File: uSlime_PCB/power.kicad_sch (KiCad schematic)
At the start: 20 parts, among them CN2 1.25T-2AW, J1 USB_C_Receptacle_USB2.0_14P, U2 MSK-12C02_SMD_SPDT_SWITCH, U3 AP2112K-3.3TRG1, U4 MCP73831T-2ACI/OT

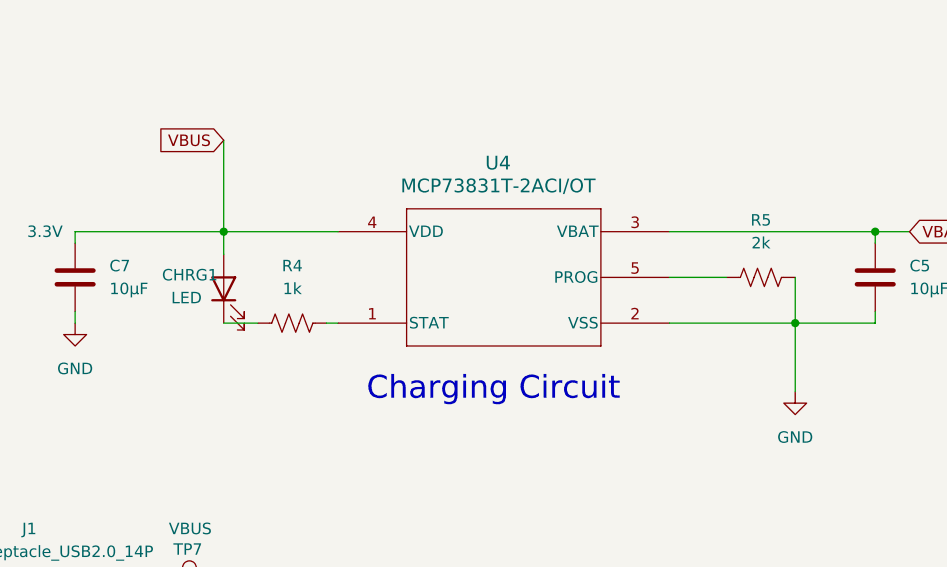
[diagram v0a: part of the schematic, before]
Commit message: v1.0.0 - Use 1206 LED, add resistor pack suggestion
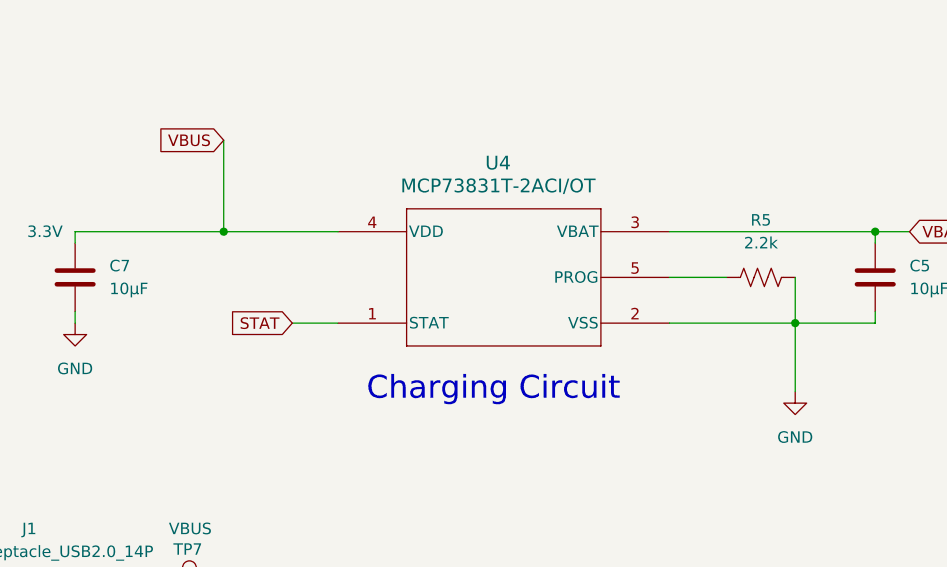
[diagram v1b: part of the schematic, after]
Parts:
- removed CHRG1: LED, LED_SMD:LED_0402_1005Metric, symbol uSlime:LED
- removed R4: 1k, Resistor_SMD:R_0402_1005Metric, symbol uSlime:R_US
- R5: value 2k -> 2.2k
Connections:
- net STAT: now reaches U4.1 (STAT)
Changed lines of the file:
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@@
-	(wire
-		(pts
-			(xy 170.18 87.63) (xy 173.99 87.63)
-		)
-		(stroke
-			(width 0)
-			(type default)
-		)
-	)
 	(wire
 		(pts
@@
 	(wire
 		(pts
-			(xy 181.61 87.63) (xy 182.88 87.63)
+			(xy 177.8 87.63) (xy 182.88 87.63)
 		)
 		(stroke
@@
 			(width 0.1524)
 			(type solid)
-		)
-	)
-	(wire
-		(pts
-			(xy 170.18 80.01) (xy 170.18 77.47)
-		)
-		(stroke
-			(width 0)
-			(type default)
 		)
 	)
@@
 		)
 	)
+	(global_label "STAT"
+		(shape input)
+		(at 177.8 87.63 180)
+		(fields_autoplaced yes)
+		(effects
+			(font
+				(size 1.27 1.27)
+			)
+			(justify right)
+		)
+		(property "Intersheetrefs" "${INTERSHEET_REFS}"
+			(at 170.5815 87.63 0)
+			(effects
+				(font
+					(size 1.27 1.27)
+				)
+				(justify right)
+				(hide yes)
+			)
+		)
+	)
 	(global_label "VBUS"
 		(shape input)
@@
 				(justify left)
 				(hide yes)
-			)
-		)
-	)
-	(symbol
-		(lib_id "uSlime:R_US")
-		(at 177.8 87.63 90)
-		(unit 1)
-		(exclude_from_sim no)
-		(in_bom yes)
-		(on_board yes)
-		(dnp no)
-		(fields_autoplaced yes)
-		(property "Reference" "R4"
-			(at 177.8 81.28 90)
-			(effects
-				(font
-					(size 1.27 1.27)
-				)
-			)
-		)
-		(property "Value" "1k"
-			(at 177.8 83.82 90)
-			(effects
-				(font
-					(size 1.27 1.27)
-				)
-			)
-		)
-		(property "Footprint" "Resistor_SMD:R_0402_1005Metric"
-			(at 178.054 86.614 90)
-			(effects
-				(font
-					(size 1.27 1.27)
-				)
-				(hide yes)
-			)
-		)
-		(property "Datasheet" "~"
-			(at 177.8 87.63 0)
-			(effects
-				(font
-					(size 1.27 1.27)
-				)
-				(hide yes)
-			)
-		)
-		(property "Description" "Resistor, US symbol"
-			(at 177.8 87.63 0)
-			(effects
-				(font
-					(size 1.27 1.27)
-				)
-				(hide yes)
-			)
-		)
-		(pin "2"
-		)
-		(pin "1"
-		)
-		(instances
-			(project "uSlime"
-				(path "/f32c1c49-f803-4e7c-a530-6db148a7ba36/9141278c-15a6-43aa-8c9d-f1bdf7efadba"
-					(reference "R4")
-					(unit 1)
-				)
 			)
 		)
@@
 	)
 	(symbol
-		(lib_id "uSlime:LED")
-		(at 170.18 83.82 90)
-		(unit 1)
-		(exclude_from_sim no)
-		(in_bom yes)
-		(on_board yes)
-		(dnp no)
-		(property "Reference" "CHRG1"
-			(at 163.322 82.296 90)
-			(effects
-				(font
-					(size 1.27 1.27)
-				)
-				(justify right)
-			)
-		)
-		(property "Value" "LED"
-			(at 164.338 84.836 90)
-			(effects
-				(font
-					(size 1.27 1.27)
-				)
-				(justify right)
-			)
-		)
-		(property "Footprint" "LED_SMD:LED_0402_1005Metric"
-			(at 170.18 83.82 0)
-			(effects
-				(font
-					(size 1.27 1.27)
-				)
-				(hide yes)
-			)
-		)
-		(property "Datasheet" "~"
-			(at 170.18 83.82 0)
-			(effects
-				(font
-					(size 1.27 1.27)
-				)
-				(hide yes)
-			)
-		)
-		(property "Description" "Light emitting diode"
-			(at 170.18 83.82 0)
-			(effects
-				(font
-					(size 1.27 1.27)
-				)
-				(hide yes)
-			)
-		)
-		(pin "1"
-		)
-		(pin "2"
-		)
-		(instances
-			(project "uSlime"
-				(path "/f32c1c49-f803-4e7c-a530-6db148a7ba36/9141278c-15a6-43aa-8c9d-f1bdf7efadba"
-					(reference "CHRG1")
-					(unit 1)
-				)
-			)
-		)
-	)
-	(symbol
 		(lib_id "uSlime:C")
 		(at 111.76 82.55 0)
@@
 			)
 		)
-		(property "Value" "2k"
+		(property "Value" "2.2k"
 			(at 229.87 78.74 90)
 			(effects

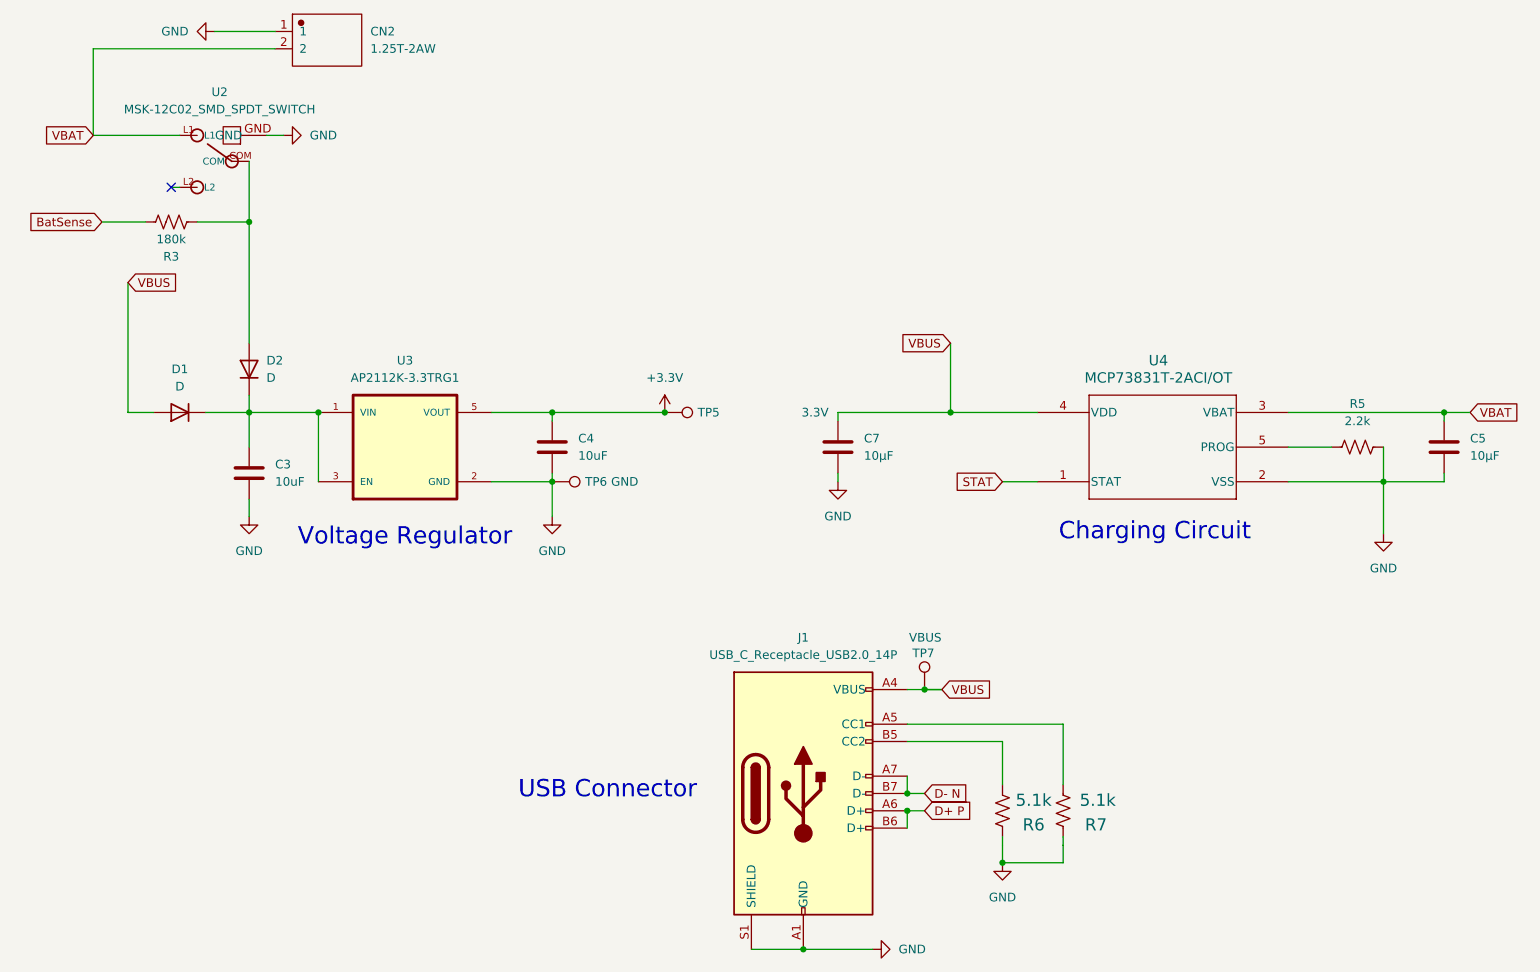
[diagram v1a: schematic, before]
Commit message: Remove GPIO9 capacitor causing boot problems
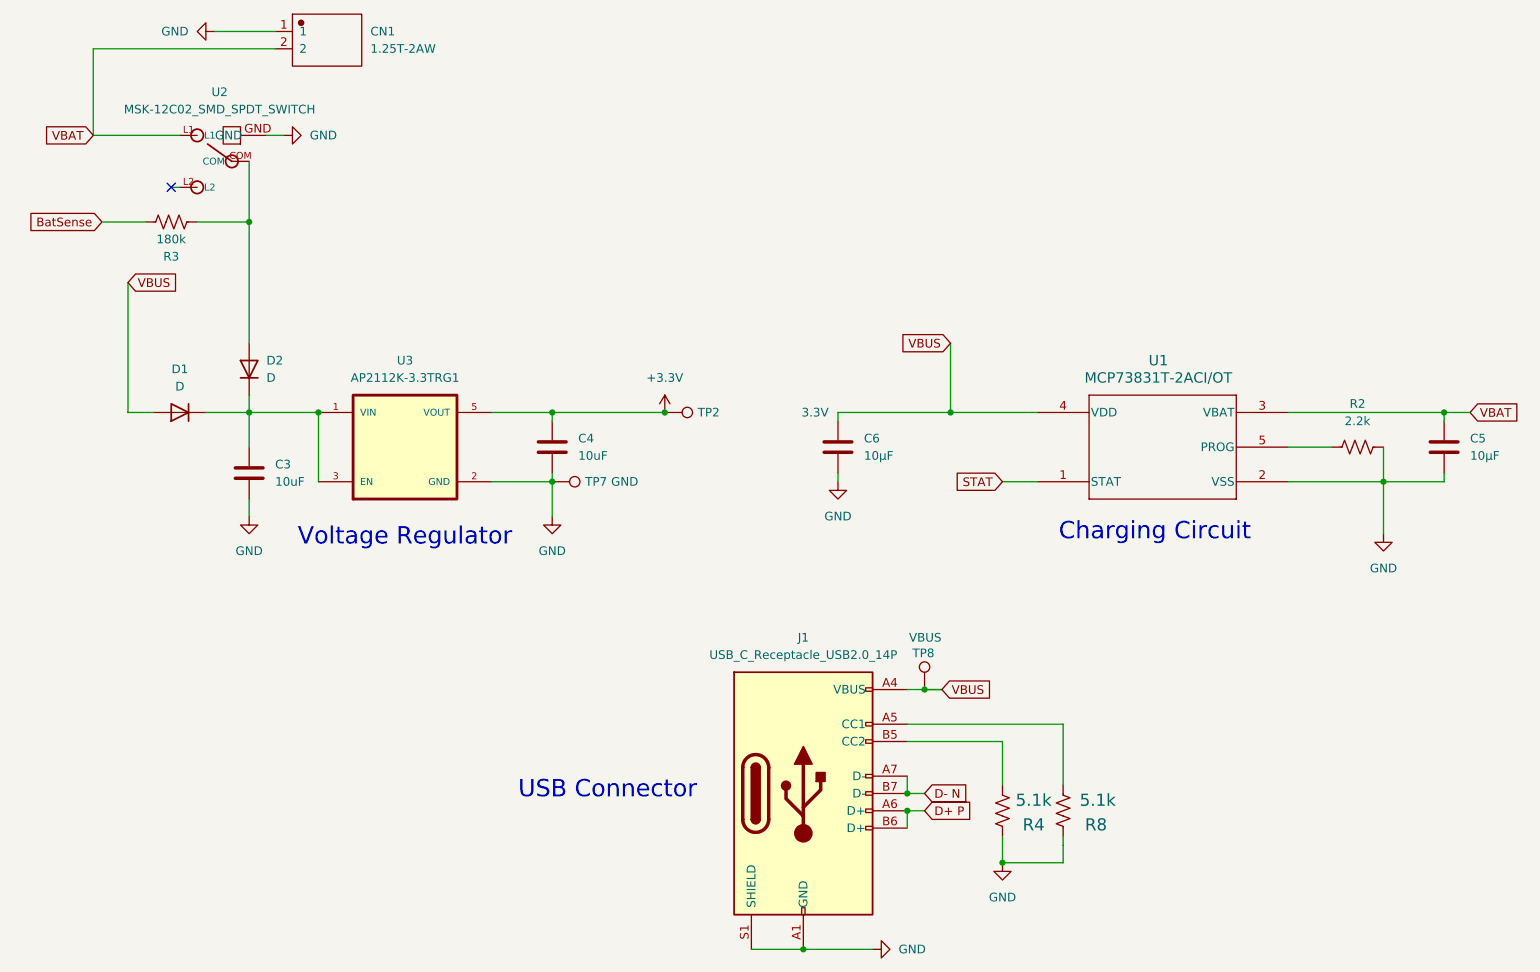
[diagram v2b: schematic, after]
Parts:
- renumbered C7 to C6, CN2 to CN1, R5 to R2, R6 to R4, R7 to R8, TP5 to TP2, TP6 to TP7, TP7 to TP8, U4 to U1
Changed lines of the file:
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@@
 		(on_board yes)
 		(dnp no)
-		(property "Reference" "U4"
+		(property "Reference" "U1"
 			(at 200.66 69.85 0)
 			(effects
@@
 			(project "uSlime"
 				(path "/f32c1c49-f803-4e7c-a530-6db148a7ba36/9141278c-15a6-43aa-8c9d-f1bdf7efadba"
-					(reference "U4")
+					(reference "U1")
 					(unit 1)
 				)
@@
 		(on_board yes)
 		(dnp no)
-		(property "Reference" "TP5"
+		(property "Reference" "TP2"
 			(at 133.096 77.47 90)
 			(effects
@@
 			(project "uSlime"
 				(path "/f32c1c49-f803-4e7c-a530-6db148a7ba36/9141278c-15a6-43aa-8c9d-f1bdf7efadba"
-					(reference "TP5")
+					(reference "TP2")
 					(unit 1)
 				)
@@
 		(on_board yes)
 		(dnp no)
-		(property "Reference" "TP6"
+		(property "Reference" "TP7"
 			(at 116.586 87.63 90)
 			(effects
@@
 			(project "uSlime"
 				(path "/f32c1c49-f803-4e7c-a530-6db148a7ba36/9141278c-15a6-43aa-8c9d-f1bdf7efadba"
-					(reference "TP6")
+					(reference "TP7")
 					(unit 1)
 				)
@@
 		(on_board yes)
 		(dnp no)
-		(property "Reference" "R7"
+		(property "Reference" "R8"
 			(at 191.516 136.906 0)
 			(effects
@@
 			(project "uSlime"
 				(path "/f32c1c49-f803-4e7c-a530-6db148a7ba36/9141278c-15a6-43aa-8c9d-f1bdf7efadba"
-					(reference "R7")
+					(reference "R8")
 					(unit 1)
 				)
@@
 		(on_board yes)
 		(dnp no)
-		(property "Reference" "TP7"
+		(property "Reference" "TP8"
 			(at 164.592 112.776 0)
 			(effects
@@
 			(project "uSlime"
 				(path "/f32c1c49-f803-4e7c-a530-6db148a7ba36/9141278c-15a6-43aa-8c9d-f1bdf7efadba"
-					(reference "TP7")
+					(reference "TP8")
 					(unit 1)
 				)
@@
 		(dnp no)
 		(fields_autoplaced yes)
-		(property "Reference" "R5"
+		(property "Reference" "R2"
 			(at 229.87 76.2 90)
 			(effects
@@
 			(project "uSlime"
 				(path "/f32c1c49-f803-4e7c-a530-6db148a7ba36/9141278c-15a6-43aa-8c9d-f1bdf7efadba"
-					(reference "R5")
+					(reference "R2")
 					(unit 1)
 				)
@@
 		(dnp no)
 		(fields_autoplaced yes)
-		(property "Reference" "CN2"
+		(property "Reference" "CN1"
 			(at 85.09 21.5899 0)
 			(effects
@@
 			(project "uSlime"
 				(path "/f32c1c49-f803-4e7c-a530-6db148a7ba36/9141278c-15a6-43aa-8c9d-f1bdf7efadba"
-					(reference "CN2")
+					(reference "CN1")
 					(unit 1)
 				)
@@
 		(on_board yes)
 		(dnp no)
-		(property "Reference" "R6"
+		(property "Reference" "R4"
 			(at 182.372 136.906 0)
 			(effects
@@
 			(project "uSlime"
 				(path "/f32c1c49-f803-4e7c-a530-6db148a7ba36/9141278c-15a6-43aa-8c9d-f1bdf7efadba"
-					(reference "R6")
+					(reference "R4")
 					(unit 1)
 				)
@@
 		(dnp no)
 		(fields_autoplaced yes)
-		(property "Reference" "C7"
+		(property "Reference" "C6"
 			(at 157.48 81.2799 0)
 			(effects
@@
 			(project "uSlime"
 				(path "/f32c1c49-f803-4e7c-a530-6db148a7ba36/9141278c-15a6-43aa-8c9d-f1bdf7efadba"
-					(reference "C7")
-					(unit 1)
-				)
+					(reference "C6")
+					(unit 1)
+				)

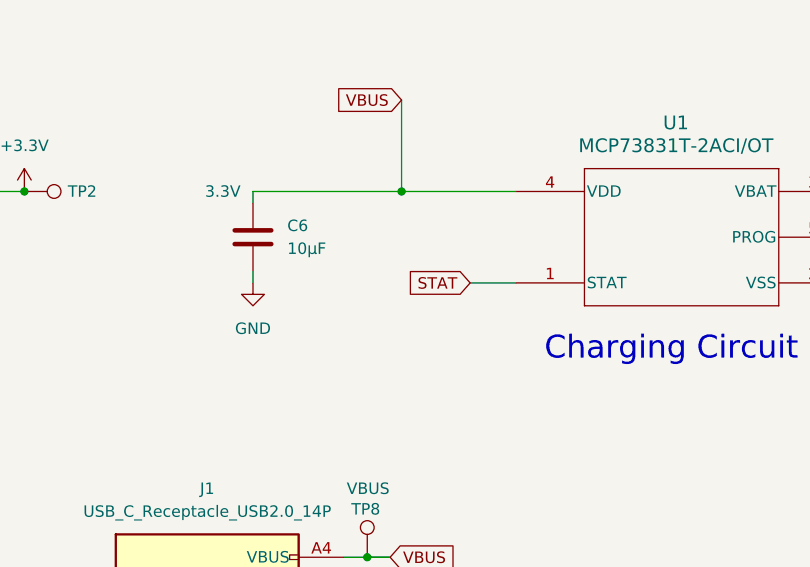
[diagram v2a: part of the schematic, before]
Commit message: v1.1.0 - Add 603 LED and resistor for charger status
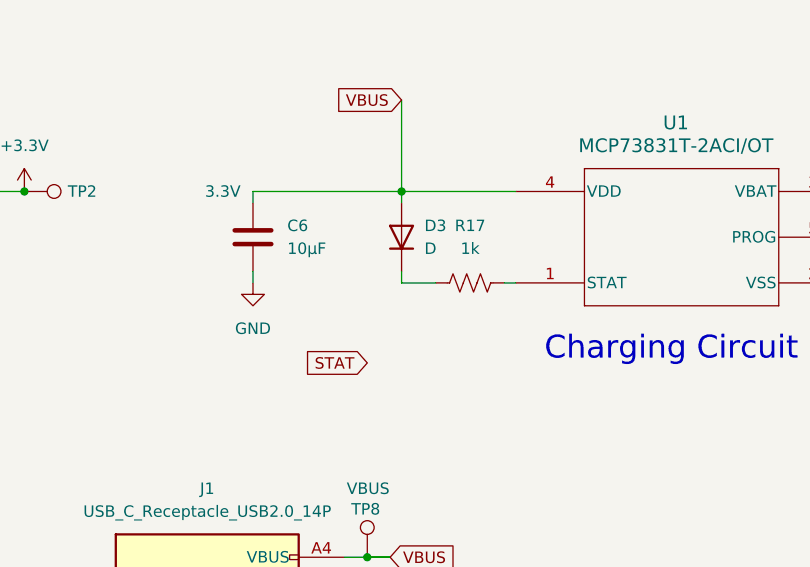
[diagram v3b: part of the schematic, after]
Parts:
- added D3: D, Diode_SMD:D_0603_1608Metric, symbol uSlime:D
- added R17: 1k, Resistor_SMD:R_0402_1005Metric, symbol uSlime:R_US
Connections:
- net STAT: no longer U1.1 (STAT)
- net VBUS: now also D3.2 (A)
- new net: R17.2, U1.1 (STAT)
- new net: D3.1 (K), R17.1
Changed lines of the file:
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@@
+	(wire
+		(pts
+			(xy 181.61 87.63) (xy 182.88 87.63)
+		)
+		(stroke
+			(width 0)
+			(type default)
+		)
+	)
 	(wire
 		(pts
@@
 		(pts
 			(xy 168.91 118.11) (xy 166.37 118.11)
+		)
+		(stroke
+			(width 0)
+			(type default)
+		)
+	)
+	(wire
+		(pts
+			(xy 170.18 86.36) (xy 170.18 87.63)
 		)
 		(stroke
@@
 	(wire
 		(pts
-			(xy 177.8 87.63) (xy 182.88 87.63)
+			(xy 170.18 87.63) (xy 173.99 87.63)
 		)
 		(stroke
@@
 		(pts
 			(xy 233.68 87.63) (xy 233.68 95.25)
+		)
+		(stroke
+			(width 0)
+			(type default)
+		)
+	)
+	(wire
+		(pts
+			(xy 170.18 78.74) (xy 170.18 77.47)
 		)
 		(stroke
@@
 		)
 	)
+	(global_label "STAT"
+		(shape input)
+		(at 166.37 96.52 180)
+		(fields_autoplaced yes)
+		(effects
+			(font
+				(size 1.27 1.27)
+			)
+			(justify right)
+		)
+		(property "Intersheetrefs" "${INTERSHEET_REFS}"
+			(at 159.1515 96.52 0)
+			(effects
+				(font
+					(size 1.27 1.27)
+				)
+				(justify right)
+				(hide yes)
+			)
+		)
+	)
 	(global_label "BatSense"
 		(shape input)
@@
 		)
 	)
-	(global_label "STAT"
+	(global_label "VBUS"
 		(shape input)
-		(at 177.8 87.63 180)
+		(at 49.53 58.42 0)
 		(fields_autoplaced yes)
 		(effects
@@
 				(size 1.27 1.27)
 			)
-			(justify right)
+			(justify left)
 		)
 		(property "Intersheetrefs" "${INTERSHEET_REFS}"
-			(at 170.5815 87.63 0)
-			(effects
-				(font
-					(size 1.27 1.27)
-				)
-				(justify right)
+			(at 57.4138 58.42 0)
+			(effects
+				(font
+					(size 1.27 1.27)
+				)
+				(justify left)
 				(hide yes)
 			)
@@
 	(global_label "VBUS"
 		(shape input)
-		(at 49.53 58.42 0)
+		(at 168.91 118.11 0)
 		(fields_autoplaced yes)
 		(effects
@@
 		)
 		(property "Intersheetrefs" "${INTERSHEET_REFS}"
-			(at 57.4138 58.42 0)
-			(effects
-				(font
-					(size 1.27 1.27)
-				)
-				(justify left)
-				(hide yes)
-			)
-		)
-	)
-	(global_label "VBUS"
-		(shape input)
-		(at 168.91 118.11 0)
-		(fields_autoplaced yes)
-		(effects
-			(font
-				(size 1.27 1.27)
-			)
-			(justify left)
-		)
-		(property "Intersheetrefs" "${INTERSHEET_REFS}"
 			(at 176.7938 118.11 0)
 			(effects
@@
 	)
 	(symbol
+		(lib_name "D_1")
+		(lib_id "uSlime:D")
+		(at 170.18 82.55 90)
+		(unit 1)
+		(exclude_from_sim no)
+		(in_bom yes)
+		(on_board yes)
+		(dnp no)
+		(fields_autoplaced yes)
+		(property "Reference" "D3"
+			(at 172.72 81.2799 90)
+			(effects
+				(font
+					(size 1.27 1.27)
+				)
+				(justify right)
+			)
+		)
+		(property "Value" "D"
+			(at 172.72 83.8199 90)
+			(effects
+				(font
+					(size 1.27 1.27)
+				)
+				(justify right)
+			)
+		)
+		(property "Footprint" "Diode_SMD:D_0603_1608Metric"
+			(at 170.18 82.55 0)
+			(effects
+				(font
+					(size 1.27 1.27)
+				)
+				(hide yes)
+			)
+		)
+		(property "Datasheet" "~"
+			(at 170.18 82.55 0)
+			(effects
+				(font
+					(size 1.27 1.27)
+				)
+				(hide yes)
+			)
+		)
+		(property "Description" "Diode"
+			(at 170.18 82.55 0)
+			(effects
+				(font
+					(size 1.27 1.27)
+				)
+				(hide yes)
+			)
+		)
+		(property "Sim.Device" "D"
+			(at 170.18 82.55 0)
+			(effects
+				(font
+					(size 1.27 1.27)
+				)
+				(hide yes)
+			)
+		)
+		(property "Sim.Pins" "1=K 2=A"
+			(at 170.18 82.55 0)
+			(effects
+				(font
+					(size 1.27 1.27)
+				)
+				(hide yes)
+			)
+		)
+		(pin "1"
+		)
+		(pin "2"
+		)
+		(instances
+			(project ""
+				(path "/f32c1c49-f803-4e7c-a530-6db148a7ba36/9141278c-15a6-43aa-8c9d-f1bdf7efadba"
+					(reference "D3")
+					(unit 1)
+				)
+			)
+		)
+	)
+	(symbol
 		(lib_id "power:GND")
 		(at 153.67 87.63 0)
@@
 					(unit 1)
 				)
+			)
+		)
+	)
+	(symbol
+		(lib_id "uSlime:R_US")
+		(at 177.8 87.63 90)
+		(unit 1)
+		(exclude_from_sim no)
+		(in_bom yes)
+		(on_board yes)
+		(dnp no)
+		(fields_autoplaced yes)
+		(property "Reference" "R17"
+			(at 177.8 81.28 90)
+			(effects
+				(font
+					(size 1.27 1.27)
+				)
+			)
+		)
+		(property "Value" "1k"
+			(at 177.8 83.82 90)
+			(effects
+				(font
+					(size 1.27 1.27)
+				)
+			)
+		)
+		(property "Footprint" "Resistor_SMD:R_0402_1005Metric"
+			(at 178.054 86.614 90)
+			(effects
+				(font
+					(size 1.27 1.27)
+				)
+				(hide yes)
+			)
+		)
+		(property "Datasheet" "~"
+			(at 177.8 87.63 0)
+			(effects
+				(font
+					(size 1.27 1.27)
+				)
+				(hide yes)
+			)
+		)
+		(property "Description" "Resistor, US symbol"
+			(at 177.8 87.63 0)
+			(effects
+				(font
+					(size 1.27 1.27)
+				)
+				(hide yes)
+			)
+		)
+		(pin "1"
+		)
+		(pin "2"
+		)
+		(instances
+			(project "uSlime"
+				(path "/f32c1c49-f803-4e7c-a530-6db148a7ba36/9141278c-15a6-43aa-8c9d-f1bdf7efadba"
+					(reference "R17")
+					(unit 1)
+				)
